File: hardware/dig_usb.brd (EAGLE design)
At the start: 146.1 x 102.6 mm, 182 parts, among them IC101 AT90USB1287-AU, IC102 MAX487CSA, IC103 74HC166D, IC301 LTV-356T, IC302 LTV-356T, IC303 LTV-356T, IC304 LTV-356T, IC305 LTV-356T, IC306 LTV-356T, IC307 LTV-356T, IC308 LTV-356T, IC401 DS1337S, K401 S202S02, K402 S202S02, K403 S202S02, K404 S202S02, K405 S202S02, K406 S202S02, K407 S202S02, K408 S202S02, Q101 16MHz, Q301 BCR191, Q302 BCR191, Q303 BCR191, Q304 BCR191, Q305 BCR191, Q306 BCR191, Q307 BCR191, Q308 BCR191, Q401 32,768kHz, X102 ISP, X308 AKL_230-08, X406 AKL_230-08

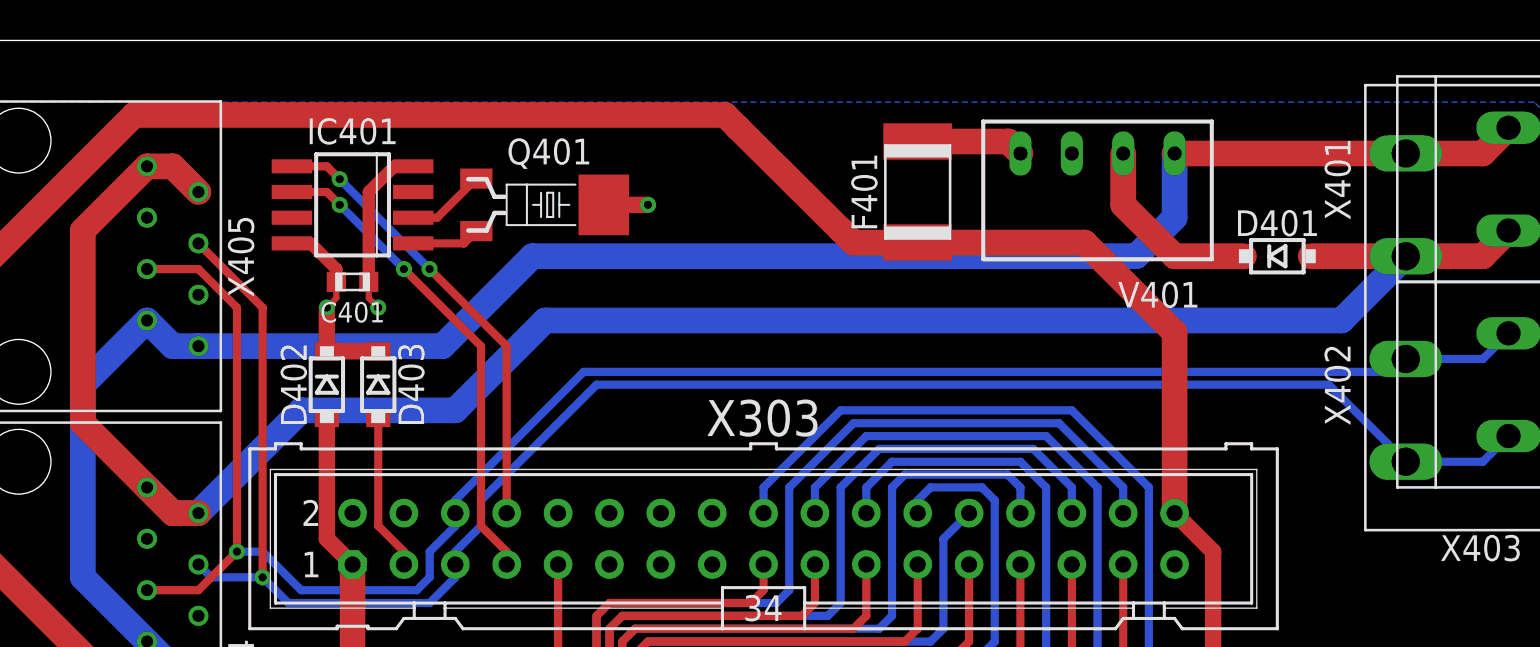
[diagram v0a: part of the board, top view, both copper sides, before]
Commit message: Alternativer DC/DC Wandler und Ausgangsfilter hinzugefügt
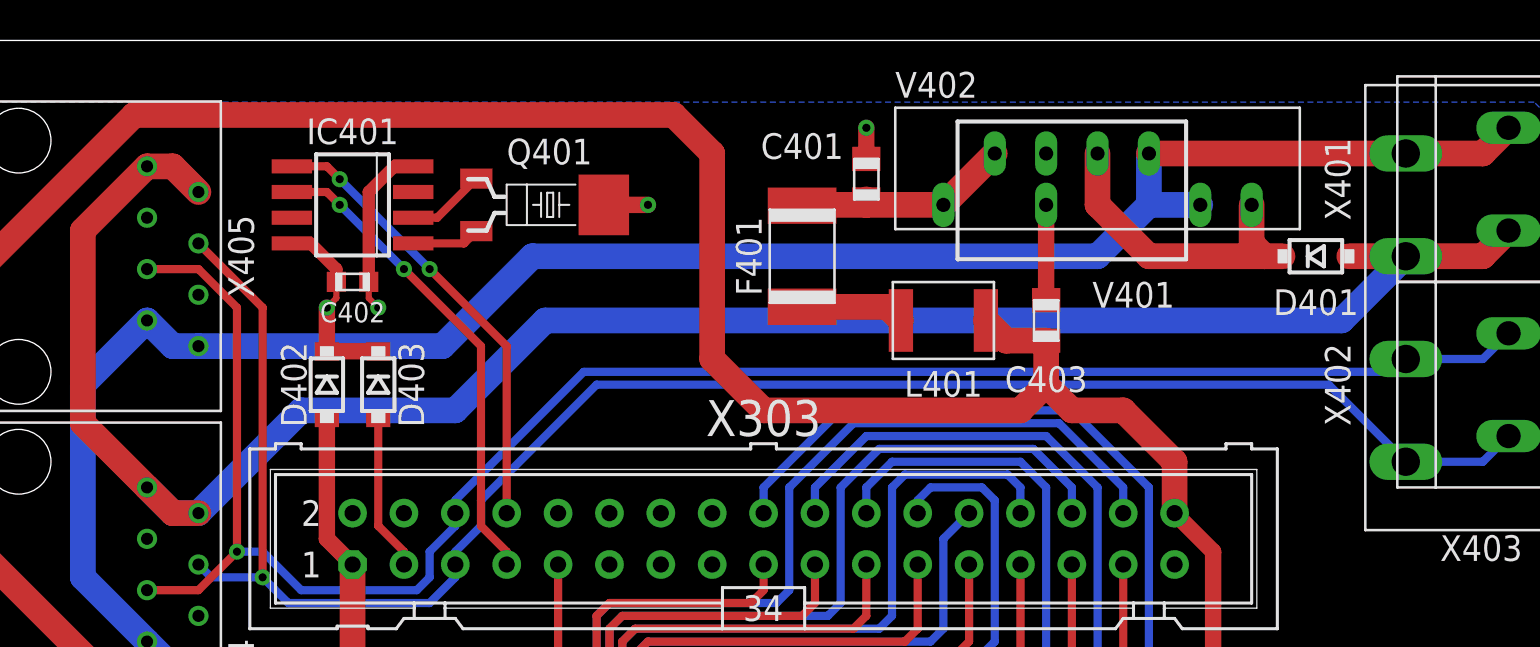
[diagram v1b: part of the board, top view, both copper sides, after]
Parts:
- added C402: 100nF, passiv:CHIP_0603
- added C403: 4,7μF, passiv:CHIP_0805
- added L401: 10μH, passiv:1812AF
- added V402: MEV1S2405, schaltregler:MEV1S
- C401: value 100nF -> 1μF; device passiv:CHIP_0603 -> passiv:CHIP_0805
- moved C401 25.9 mm to (49.5, 95.2), turned to 90 degrees
- moved F401 6.54 mm to (46.4, 91.4)
- moved D401 1.91 mm to (71.8, 91.4)
- moved V401 1.27 mm to (59.7, 96.5)
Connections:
- removed net N$41: F401.2, V401.4
- new net N$19: C401.1, F401.2, V401.4, V402.7
- new net N$24: F401.1, L401.2
- net +5V: now also C403.1, L401.1; no longer F401.1
- net GND: now also C402.2, C403.2, V402.5
- net N$23: now also V402.1
- net N$64: now also C402.1; no longer C401.1
- net V-: now also V402.2
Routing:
- net N$19: track 0.00 -> 10.9 mm
- net +5V: track 727.2 -> 736.0 mm
- net GND: track 134.7 -> 140.9 mm, vias 41 -> 42
- net N$23: track 9.56 -> 15.5 mm
- net N$41: track 5.33 -> 0.00 mm
- net N$24: track 0.00 -> 5.16 mm
- net V-: track 95.7 -> 97.9 mm
- net V+: track 103.0 -> 101.1 mm

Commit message: Testpads hinzugefügt
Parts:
- added 0V, 5V, GND, N: (no value), test:VIA08
- added ADC0, ADC1, ADC2, ADC3, ADC4, ADC5, ADC6, ADC7: (no value), test:PADS
- added SCL, SDA, SGND: (no value), test:VIA06
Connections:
- new net N$148: ADC2.1, X303.11
- new net N$149: ADC3.1, X303.12
- new net N$150: ADC4.1, X303.13
- new net N$151: ADC5.1, X303.14
- new net N$152: ADC6.1, X303.15
- new net N$153: ADC7.1, X303.16
- new net N$41: ADC1.1, X303.10
- net +5V: now also 5V.1
- net GND: now also 0V.1, GND.1, SGND.1
- net GNDIO: now also N.1
- net N$131: now also SCL.1
- net N$132: now also SDA.1
- net N$146: now also ADC0.1
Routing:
- net N$151: track 0.00 -> 11.6 mm
- net N$149: track 0.00 -> 11.6 mm
- net N$153: track 0.00 -> 11.3 mm
- net N$131: track 23.8 -> 34.2 mm
- net N$41: track 0.00 -> 9.46 mm
- net N$152: track 0.00 -> 8.56 mm
- net N$150: track 0.00 -> 8.56 mm
- net N$148: track 0.00 -> 8.19 mm
- net N$146: track 19.9 -> 27.0 mm, vias 0 -> 2
- net N$132: track 22.6 -> 28.6 mm
- net N$99: track 85.0 -> 81.3 mm
- net N$98: track 71.4 -> 67.7 mm
- net N$101: track 106.7 -> 102.9 mm
- net N$88: track 61.8 -> 58.1 mm
- net N$87: track 53.3 -> 49.6 mm
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
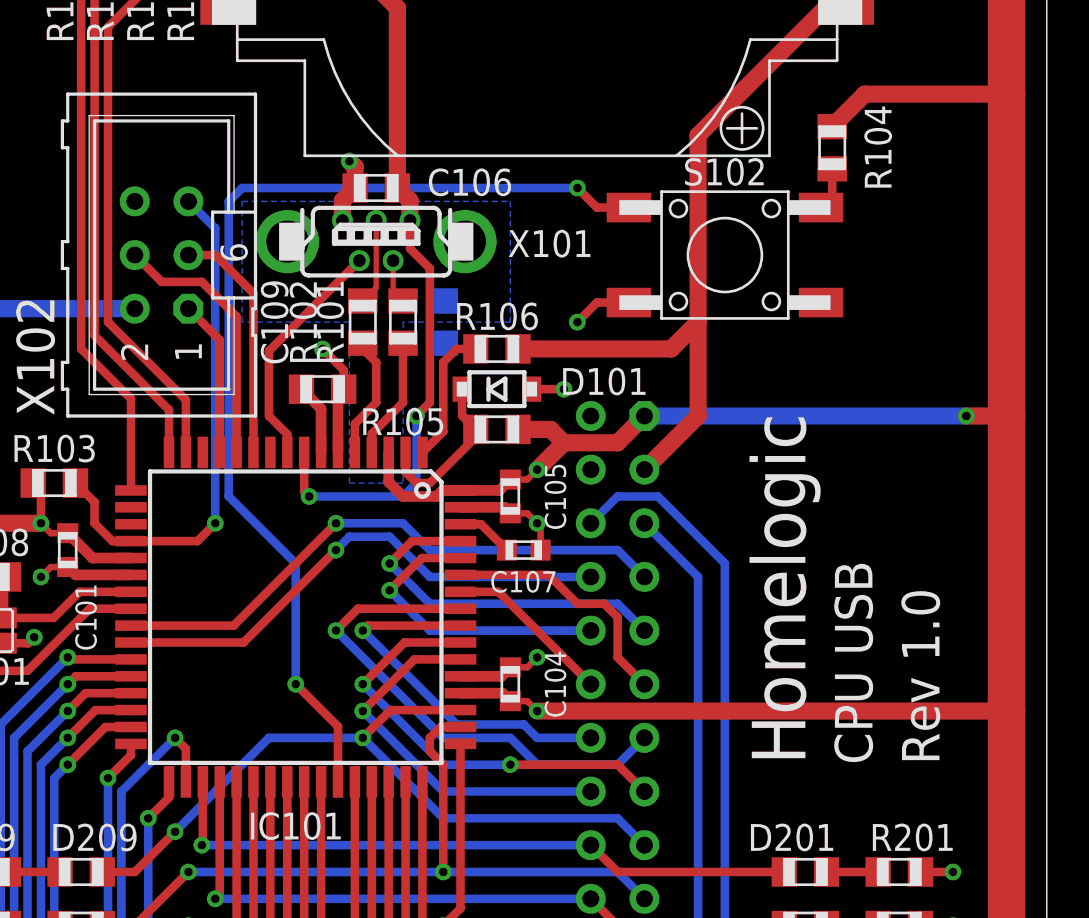
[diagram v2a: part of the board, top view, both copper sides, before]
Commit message: Zusätzlicher Kondensator für UVcc; HWB mit INT4 verbunden
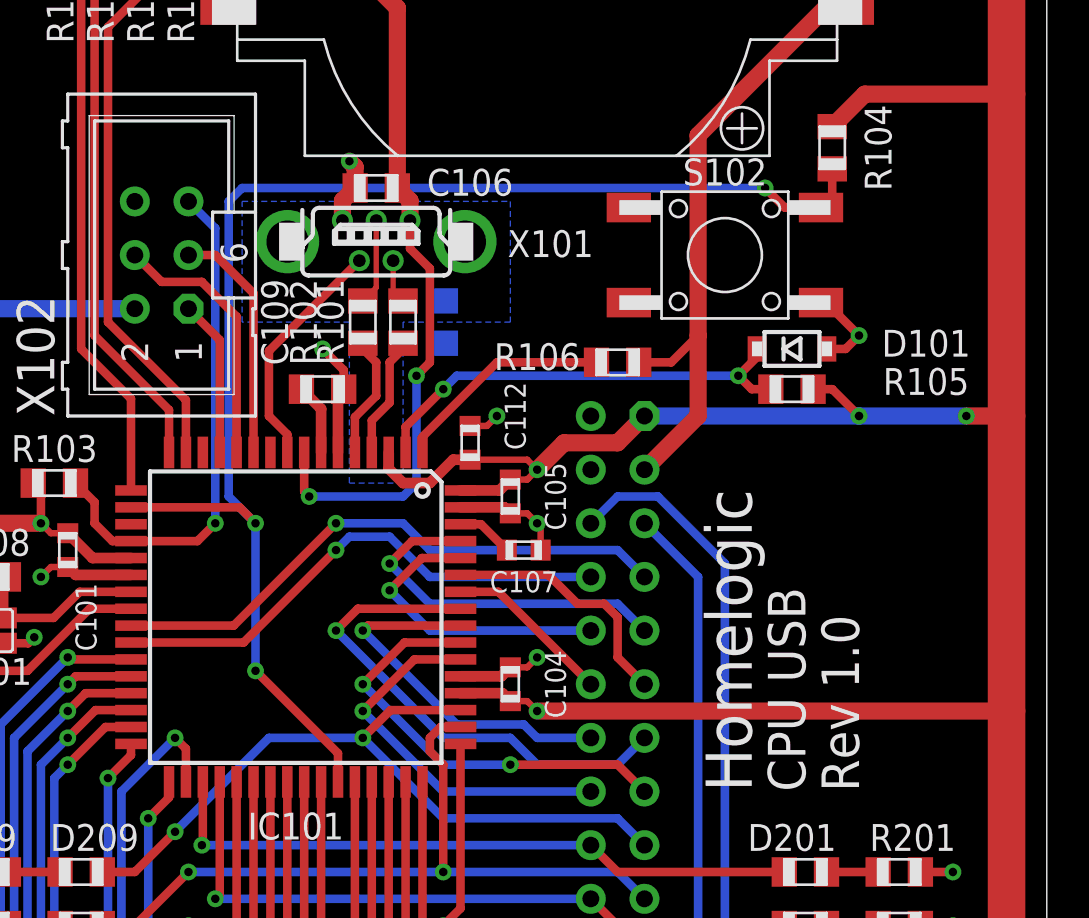
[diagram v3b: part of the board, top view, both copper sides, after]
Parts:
- added C112: 100nF, passiv:CHIP_0603
- moved D101 14.1 mm to (134.0, 71.8)
- moved R105 14.1 mm to (134.0, 69.8)
- moved R106 5.75 mm to (125.7, 71.1)
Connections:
- net +5V: now also C112.1
- net GND: now also C112.2
- net N$147: now also IC101.18
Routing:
- net N$147: track 51.3 -> 66.6 mm, vias 2 -> 3
- net N$129: track 7.91 -> 21.4 mm, vias 0 -> 2
- net N$143: track 35.9 -> 30.2 mm
- net N$21: track 6.48 -> 10.4 mm
- net +5V: track 736.0 -> 739.8 mm, vias 16 -> 17
- net GND: track 140.9 -> 142.3 mm

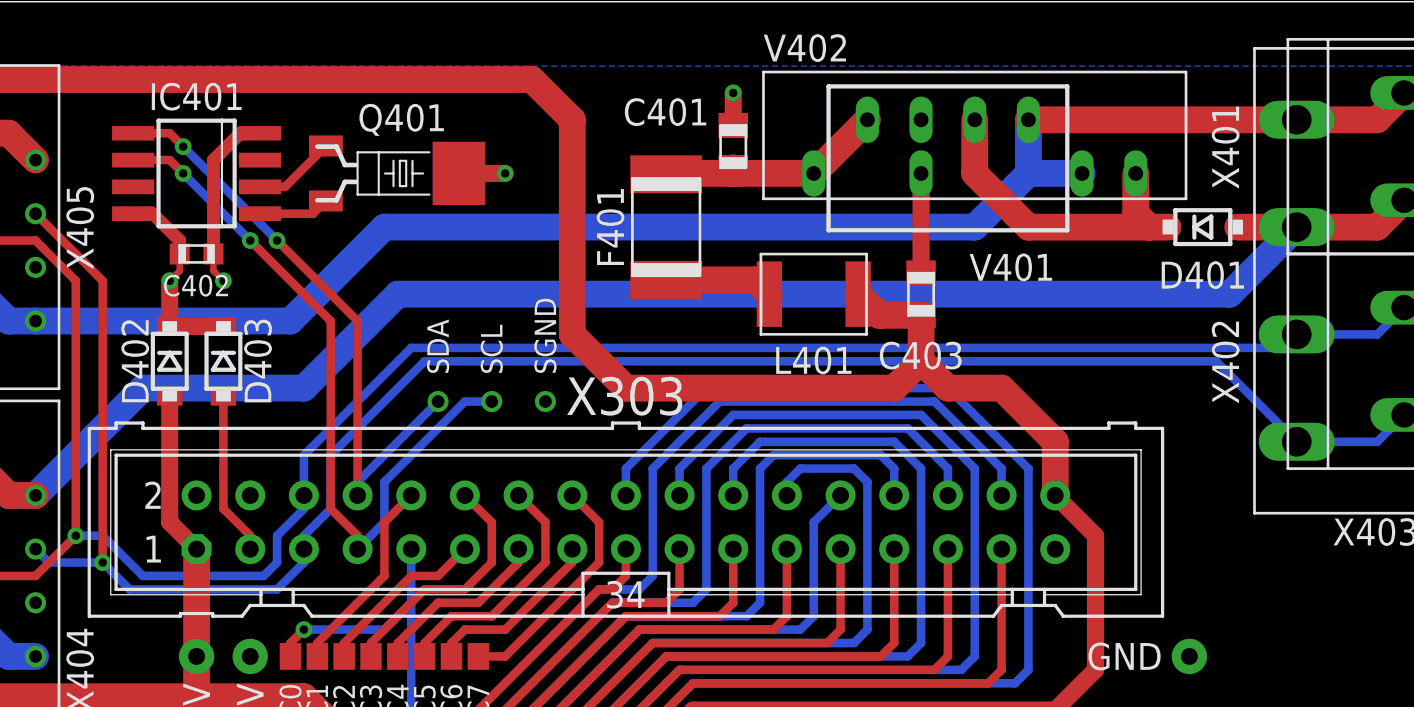
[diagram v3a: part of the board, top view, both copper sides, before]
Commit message: I2C EEPROM hinzugefügt auf dig_usb hinzugefügt
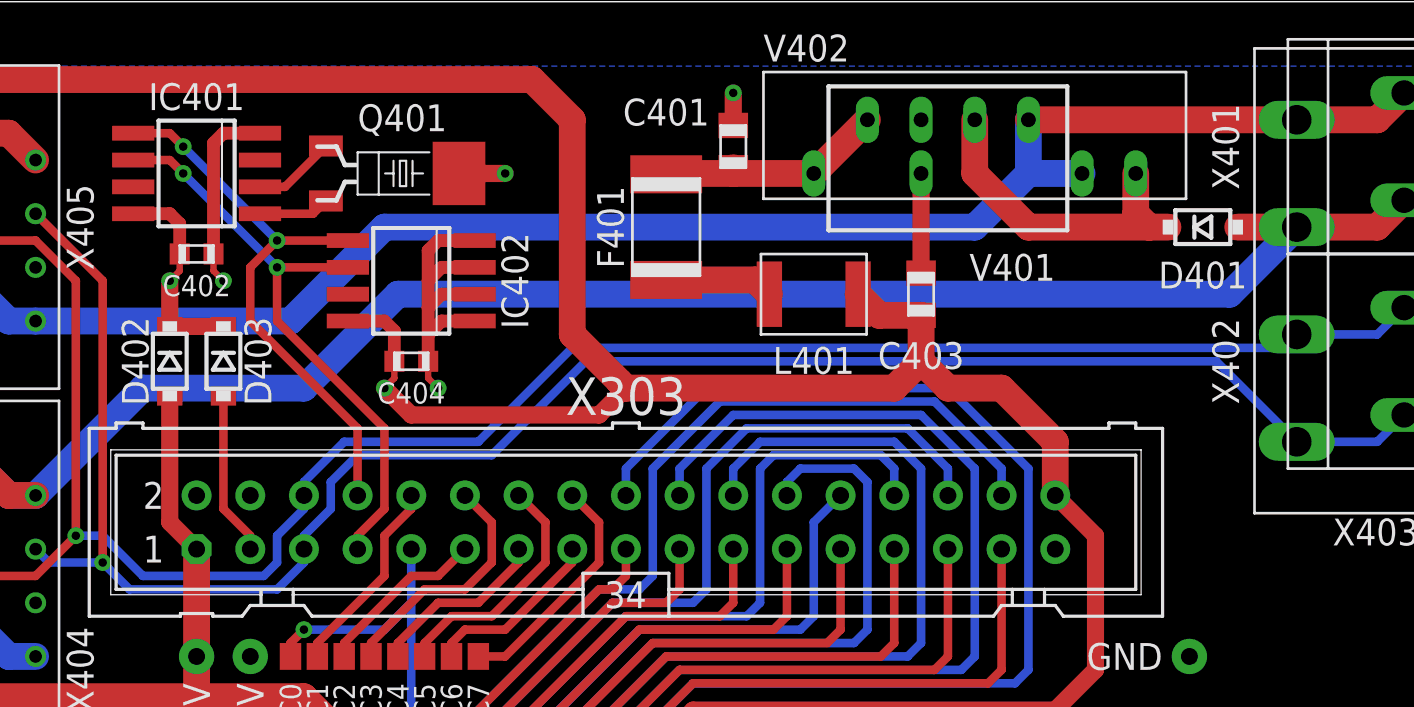
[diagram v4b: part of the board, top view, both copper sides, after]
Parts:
- removed SCL, SDA, SGND: (no value), test:VIA06
- added C404: 100nF, passiv:CHIP_0603
- added IC402: M24C01WMN, ic-speicher:SOP08_127
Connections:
- net +5V: now also C404.1, IC402.8
- net GND: now also C404.2, IC402.1, IC402.2, IC402.3, IC402.4; no longer SGND.1
- net N$131: now also IC402.6; no longer SCL.1
- net N$132: now also IC402.5; no longer SDA.1
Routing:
- net +5V: track 739.8 -> 757.8 mm, vias 17 -> 18
- net GND: track 142.3 -> 159.2 mm, vias 42 -> 43
- net N$131: track 34.2 -> 28.2 mm
- net N$132: track 28.6 -> 27.0 mm
- net N$134: track 92.2 -> 91.4 mm
- net N$133: track 93.7 -> 92.9 mm
